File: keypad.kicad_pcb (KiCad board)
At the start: 4 copper layers, 100 x 100 mm, 84 parts, among them J1 UJ20-C-H-G-SMT-5-P16-TR, SW1 SW_SPST, SW10 SW_SPST, SW11 SW_SPST, SW12 SW_SPST, SW13 SW_SPST, SW14 SW_SPST, SW15 SW_SPST, SW16 SW_SPST, SW17 SW_SPST, SW18 SW_SPST, SW19 SW_SPST, SW2 SW_SPST, SW20 SW_SPST, SW21 SW_SPST, SW22 SW_SPST, SW23 SW_SPST, SW24 SW_SPST, SW25 SW_SPST, SW26 SW_Reset, SW3 SW_SPST, SW4 SW_SPST, SW5 SW_SPST, SW6 SW_SPST, SW7 SW_SPST, SW8 SW_SPST, SW9 SW_SPST, U1 ATmega32U4-A, Y1 LFXTAL085842

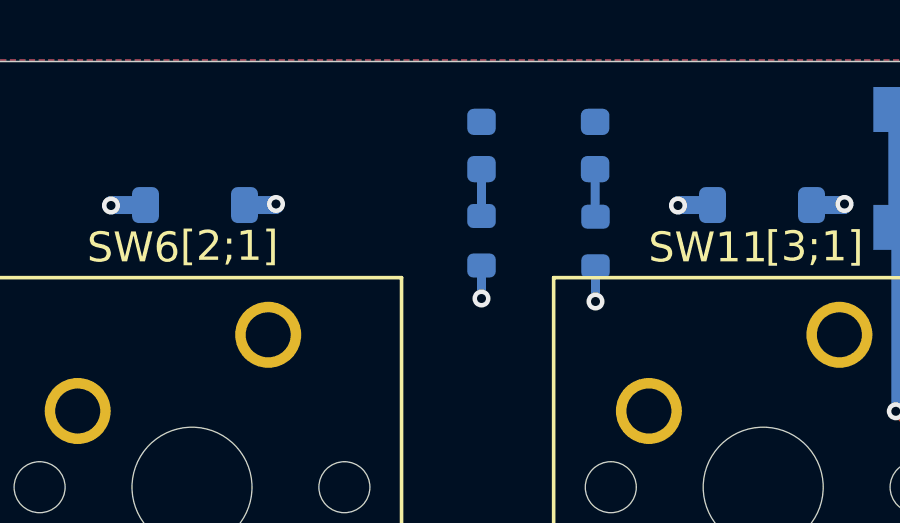
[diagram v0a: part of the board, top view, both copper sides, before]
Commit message: moved LED
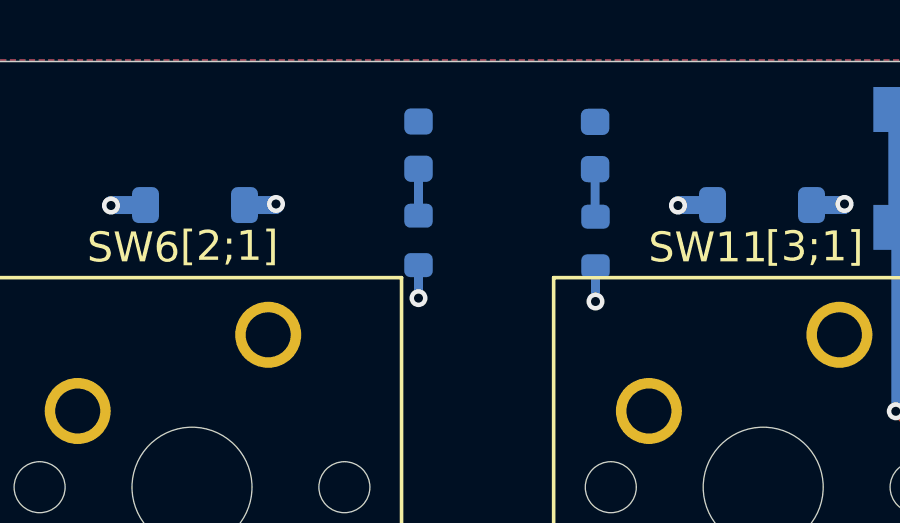
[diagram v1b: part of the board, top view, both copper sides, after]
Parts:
- moved D26 2.10 mm to (54.9, 18.0)
- moved R9 2.10 mm to (54.9, 21.2)
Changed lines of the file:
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@@
 	(footprint "Resistor_SMD:R_0603_1608Metric"
 		(layer "B.Cu")
-		(at 57 21.175 -90)
+		(at 54.9 21.1625 -90)
 		(descr "Resistor SMD 0603 (1608 Metric), square (rectangular) end terminal, IPC-7351 nominal, (Body size source: IPC-SM-782 page 72, https://www.pcb-3d.com/wordpress/wp-content/uploads/ipc-sm-782a_amendment_1_and_2.pdf), generated with kicad-footprint-generator")
 		(tags "resistor")
@@
 	(footprint "LED_SMD:LED_0603_1608Metric"
 		(layer "B.Cu")
-		(at 57 18 -90)
+		(at 54.9 17.9875 -90)
 		(descr "LED SMD 0603 (1608 Metric), square (rectangular) end terminal, IPC-7351 nominal, (Body size source: http://www.tortai-tech.com/upload/download/2011102023233369053.pdf), generated with kicad-footprint-generator")
 		(tags "LED")
@@
 	)
 	(segment
-		(start 57 18.7875)
-		(end 57 20.35)
+		(start 54.9 18.775)
+		(end 54.9 20.3375)
 		(width 0.3)
 		(layer "B.Cu")
@@
 	)
 	(via
-		(at 57 23.1)
+		(at 54.9 23.0875)
 		(size 0.6)
 		(drill 0.3)
@@
 	)
 	(segment
-		(start 57 22)
-		(end 57 23.1)
+		(start 54.9 21.9875)
+		(end 54.9 23.0875)
 		(width 0.3)
 		(layer "B.Cu")

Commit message: reversed LED change
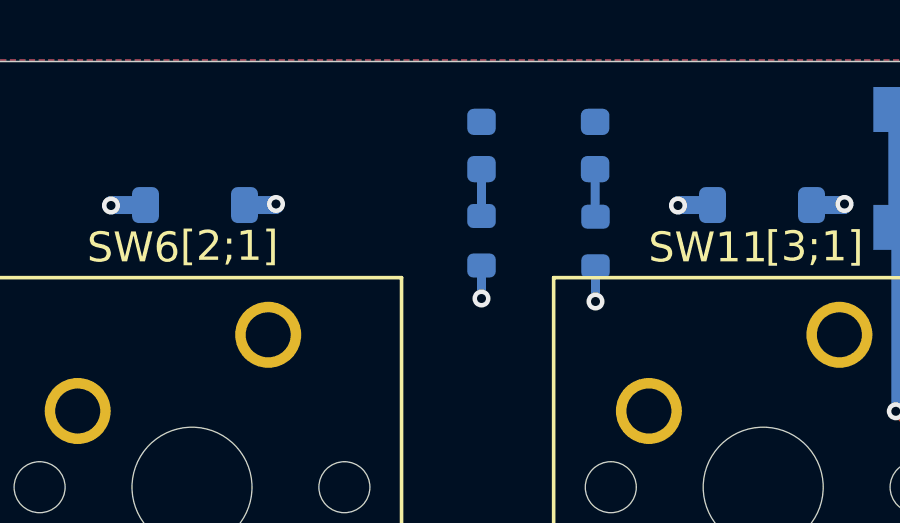
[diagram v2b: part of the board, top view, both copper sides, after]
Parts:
- moved D26 2.10 mm to (57.0, 18.0)
- moved R9 2.10 mm to (57.0, 21.2)
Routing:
- net LED2: track 22.9 -> 41.5 mm
- net LED1: track 21.1 -> 38.4 mm
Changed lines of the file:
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@@
 	(footprint "Resistor_SMD:R_0603_1608Metric"
 		(layer "B.Cu")
-		(at 54.9 21.1625 -90)
+		(at 57 21.175 -90)
 		(descr "Resistor SMD 0603 (1608 Metric), square (rectangular) end terminal, IPC-7351 nominal, (Body size source: IPC-SM-782 page 72, https://www.pcb-3d.com/wordpress/wp-content/uploads/ipc-sm-782a_amendment_1_and_2.pdf), generated with kicad-footprint-generator")
 		(tags "resistor")
@@
 	(footprint "LED_SMD:LED_0603_1608Metric"
 		(layer "B.Cu")
-		(at 54.9 17.9875 -90)
+		(at 57 18 -90)
 		(descr "LED SMD 0603 (1608 Metric), square (rectangular) end terminal, IPC-7351 nominal, (Body size source: http://www.tortai-tech.com/upload/download/2011102023233369053.pdf), generated with kicad-footprint-generator")
 		(tags "LED")
@@
 	)
 	(segment
-		(start 54.9 18.775)
-		(end 54.9 20.3375)
+		(start 57 18.7875)
+		(end 57 20.35)
 		(width 0.3)
 		(layer "B.Cu")
@@
 	)
 	(via
-		(at 54.9 23.0875)
+		(at 57 23.1)
 		(size 0.6)
 		(drill 0.3)
@@
 	)
 	(segment
-		(start 54.9 21.9875)
-		(end 54.9 23.0875)
+		(start 57 22)
+		(end 57 23.1)
 		(width 0.3)
 		(layer "B.Cu")
@@
 		(net 73)
 	)
+	(segment
+		(start 57 36.65)
+		(end 57 23.1)
+		(width 0.3)
+		(layer "In2.Cu")
+		(net 73)
+	)
+	(segment
+		(start 60.55 40.2)
+		(end 57 36.65)
+		(width 0.3)
+		(layer "In2.Cu")
+		(net 73)
+	)
 	(via
 		(at 75 46)
@@
 		(net 74)
 	)
+	(segment
+		(start 60.059 38.613481)
+		(end 61.239045 39.793526)
+		(width 0.3)
+		(layer "In2.Cu")
+		(net 74)
+	)
+	(segment
+		(start 60.059 23.941)
+		(end 60.059 38.613481)
+		(width 0.3)
+		(layer "In2.Cu")
+		(net 74)
+	)
+	(segment
+		(start 60.8 23.2)
+		(end 60.059 23.941)
+		(width 0.3)
+		(layer "In2.Cu")
+		(net 74)
+	)

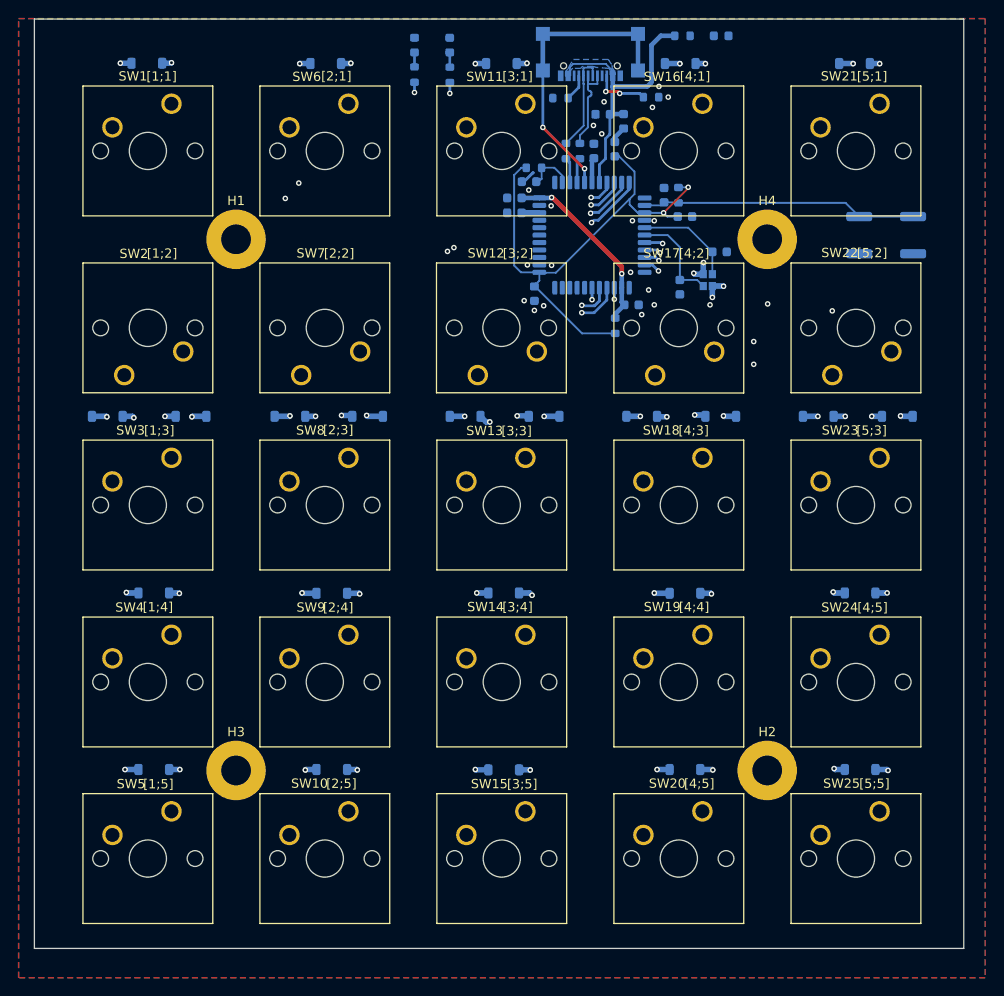
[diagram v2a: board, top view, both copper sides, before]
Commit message: switched MC to QFN, rerouted board
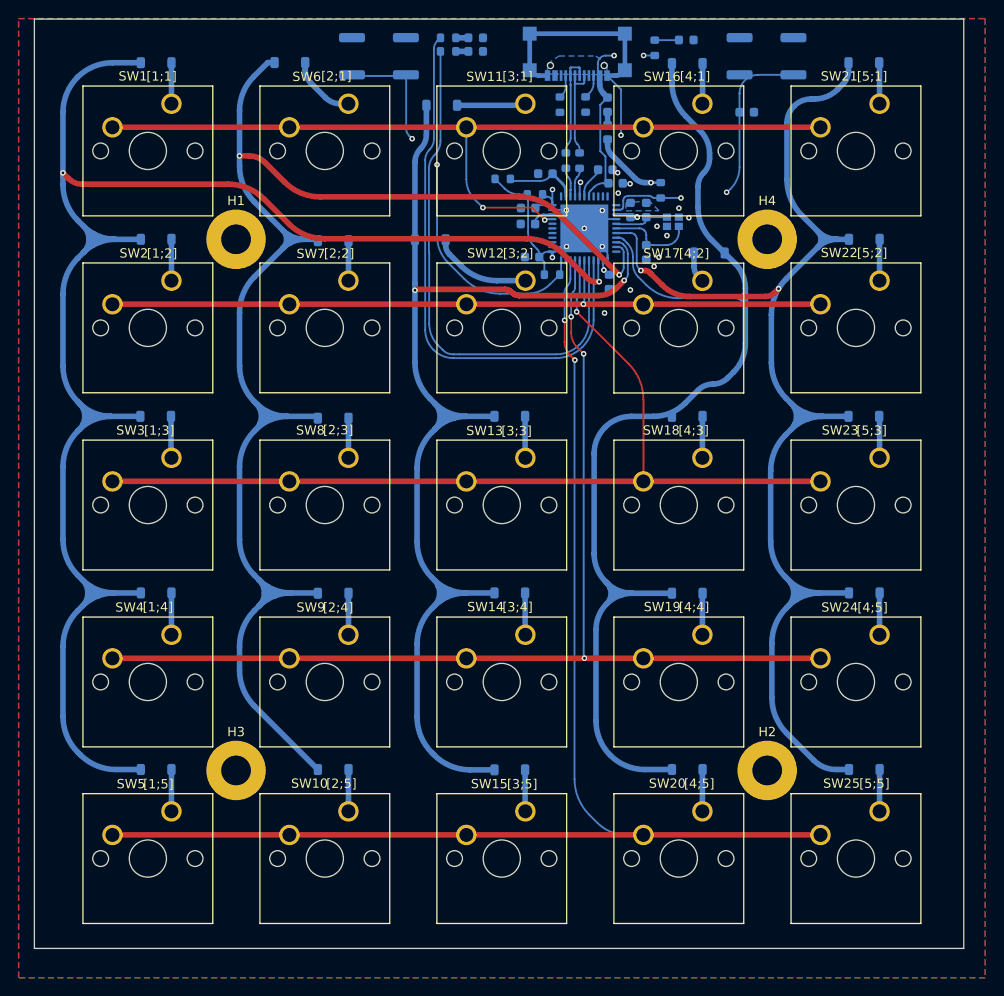
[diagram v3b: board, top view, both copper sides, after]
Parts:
- added R11: 10k, Resistor_SMD:R_0603_1608Metric, B.Cu at (71.8, 42.7)
- added SW27: SW_HWB, Button_Switch_SMD:SW_Push_1P1T_NO_CK_KSC7xxJ, B.Cu at (53.2, 19.2)
- U1: footprint Package_QFP:TQFP-44_10x10mm_P0.8mm -> Package_DFN_QFN:QFN-44-1EP_7x7mm_P0.5mm_EP5.15x5.15mm
- moved SW26 23.2 mm to (94.9, 19.2), turned to 180 degrees
- moved D12 22.6 mm to (58.7, 39.0), turned to 0 degrees
- moved D22 19.4 mm to (29.2, 38.9), turned to 0 degrees
- moved D2 19.4 mm to (105.4, 38.9), turned to 0 degrees
- moved D17 19.3 mm to (48.2, 39.0), turned to 0 degrees
- moved D7 17.6 mm to (88.7, 40.4)
- moved R3 16.6 mm to (70.0, 34.1), turned to 0 degrees
- moved C9 12.6 mm to (92.8, 25.2), turned to 0 degrees
- moved SW12 11.4 mm to (68.9, 43.4), turned to 0 degrees
- moved SW17 11.4 mm to (88.0, 43.4), turned to 0 degrees
- moved SW22 11.4 mm to (107.0, 43.4), turned to 0 degrees
- moved SW2 11.4 mm to (30.9, 43.4), turned to 0 degrees
- moved SW7 11.4 mm to (49.9, 43.4), turned to 0 degrees
- moved C13 9.08 mm to (81.9, 35.7), turned to -90 degrees
- moved D11 7.84 mm to (59.9, 24.5)
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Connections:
- net Net-(U1-D+) renamed D1+
- net Net-(U1-D-) renamed D1-
- J1 pad A1: GND -> uGND
- J1 pad B1: GND -> uGND
- U1 pad 1: E6 -> unconnected-(U1-PE6-Pad1)
- U1 pad 10: Row 3 -> unconnected-(U1-PB2-Pad10)
- U1 pad 11: Row 4 -> unconnected-(U1-PB3-Pad11)
- U1 pad 12: B7 -> unconnected-(U1-PB7-Pad12)
- U1 pad 18: Col 1 -> Row 5
- U1 pad 19: Col 2 -> Row 4
- U1 pad 20: Col 3 -> Row 3
- U1 pad 21: Col 4 -> Row 2
- U1 pad 22: D5 -> unconnected-(U1-PD5-Pad22)
- U1 pad 25: Col 5 -> Row 1
- U1 pad 26: LED2 -> LED1
- U1 pad 27: LED1 -> LED2
- U1 pad 28: Row 5 -> Col 2
- U1 pad 29: B5 -> Col 3
- U1 pad 30: B6 -> Col 4
- U1 pad 31: C6 -> Col 5
- U1 pad 32: C7 -> unconnected-(U1-PC7-Pad32)
- U1 pad 33: E2 -> HWB
- U1 pad 36: F7 -> unconnected-(U1-PF7-Pad36)
- U1 pad 37: F6 -> unconnected-(U1-PF6-Pad37)
- U1 pad 38: F5 -> unconnected-(U1-PF5-Pad38)
- U1 pad 39: F4 -> unconnected-(U1-PF4-Pad39)
- U1 pad 40: F1 -> unconnected-(U1-PF1-Pad40)
- U1 pad 41: F0 -> Col 1
- U1 pad 5: unconnected-(U1-UGND-Pad5) -> uGND
- U1 pad 8: Row 1 -> unconnected-(U1-PB0-Pad8)
- U1 pad 9: Row 2 -> unconnected-(U1-PB1-Pad9)
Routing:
- net HWB: track 0.00 -> 42.9 mm, vias 0 -> 2
- net Row 1: track 158.5 -> 199.5 mm, vias 7 -> 2
- net Row 2: track 133.6 -> 174.0 mm, vias 7 -> 2
- net Row 3: track 111.6 -> 139.9 mm, vias 6 -> 2
- net Row 5: track 122.4 -> 148.8 mm, vias 9 -> 2
- net LED1: track 38.4 -> 60.4 mm, vias 3 -> 0
- net Row 4: track 113.3 -> 131.9 mm, vias 6 -> 0
- net LED2: track 41.5 -> 57.3 mm, vias 3 -> 0
- net +5V: track 57.1 -> 41.8 mm, vias 2 -> 3
- net Col 2: track 96.2 -> 81.0 mm
- net VBUS: track 31.5 -> 23.4 mm, vias 0 -> 2
- net Col 3: track 108.0 -> 102.8 mm, vias 3 -> 1
- net uGND: track 32.0 -> 37.2 mm
- net Col 5: track 138.2 -> 143.3 mm, vias 1 -> 2
- net XTAL2: track 10.8 -> 5.88 mm
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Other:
- board text added: "Boot"
- board text added: "Reset"
- board text added: "power LED"
- board text added: "programmable status LEDs"
